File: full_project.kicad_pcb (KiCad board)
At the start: 2 copper layers, 61.4 x 86.1 mm, 40 parts, among them J1 Conn_01x16, J12 V_OFFSET, J14 Conn_01x02, J2 Raspberry_Pi_2_3, J3 Conn_01x08, J4 Screw_Terminal_01x04_titrator, J5 RF_Shield_Two_Pieces, J6 BNC_Jack, J8 Screw_Terminal_01x03, Q1 PN2222A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

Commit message: here
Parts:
- moved J6 0.77 mm to (128.0, 54.7)
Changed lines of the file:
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@@
   )
   (module Titrator_Footprints:BNC_Jack (layer F.Cu)
-    (at 127.254 54.737)
+    (at 128.025 54.675)
     (fp_text reference J6 (at 6.394 -0.443) (layer F.SilkS)
       (effects (font (size 1 1) (thickness 0.15)))
@@
   (gr_line (start 136.398 55.372) (end 136.398 27.305) (layer Dwgs.User) (width 0.15))
   (gr_line (start 161.925 27.305) (end 161.925 55.372) (layer Dwgs.User) (width 0.15))
-  (gr_line (start 161.925 55.372) (end 136.525 55.372) (layer Dwgs.User) (width 0.15))
-  (gr_line (start 188.468 55.372) (end 163.068 55.372) (layer Dwgs.User) (width 0.15))
+  (gr_line (start 161.925 55.372) (end 136.398 55.372) (layer Dwgs.User) (width 0.15))
+  (gr_line (start 188.468 55.372) (end 162.941 55.372) (layer Dwgs.User) (width 0.15))
   (gr_line (start 188.468 27.305) (end 188.468 55.372) (layer Dwgs.User) (width 0.15))
   (gr_line (start 162.941 27.305) (end 188.341 27.305) (layer Dwgs.User) (width 0.15))

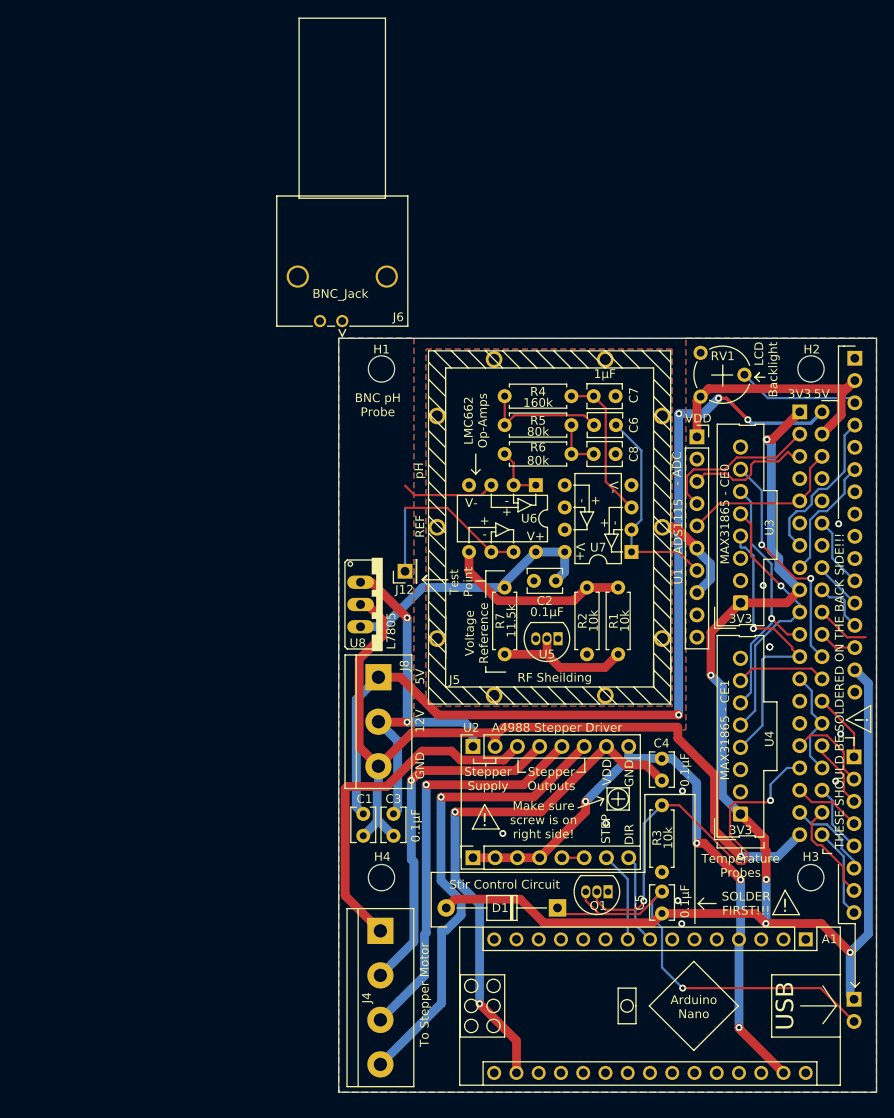
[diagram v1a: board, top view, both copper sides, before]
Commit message: Extended board, added MAX31685 footprint for new mounting style, added 3.5mm audio jacks, cried a little
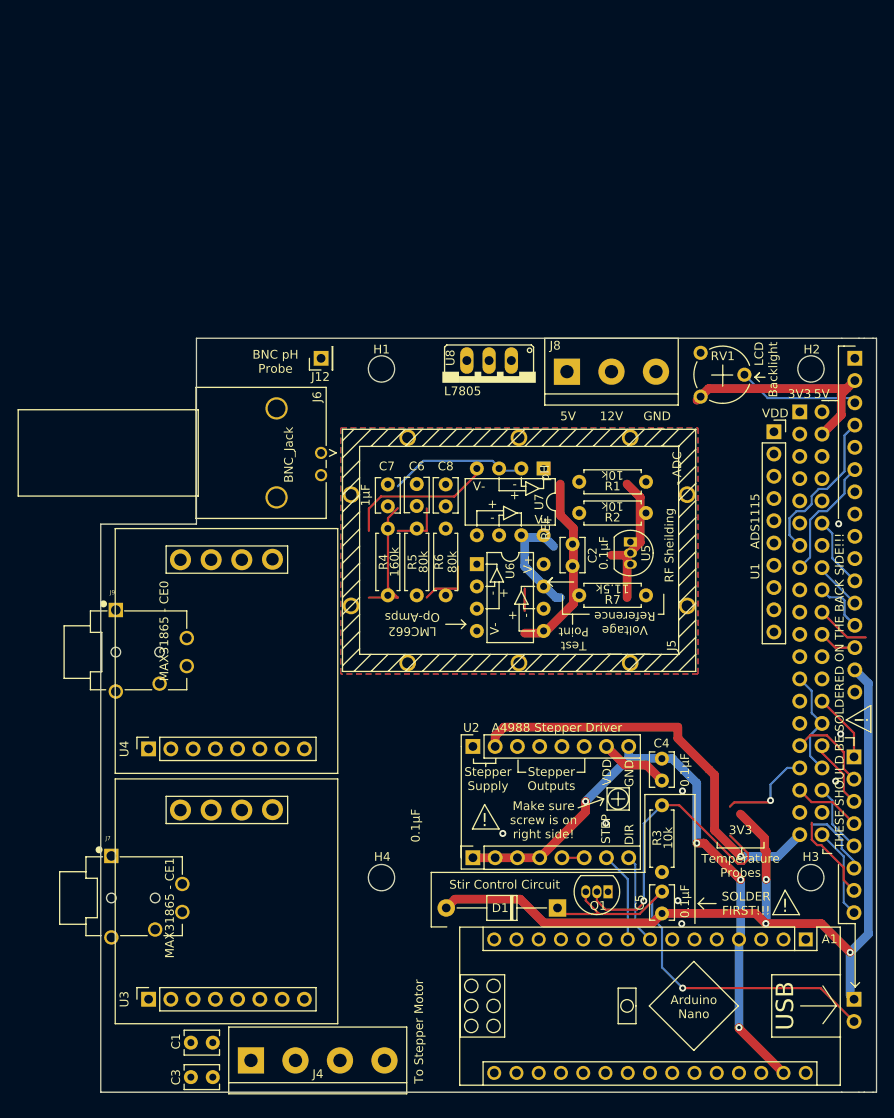
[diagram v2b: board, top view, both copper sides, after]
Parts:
- added J7: SJ-43515TS, Titrator_Footprints:CUI_SJ-43515TS, F.Cu at (104.3, 120.5)
- added J9: SJ-43515TS, Titrator_Footprints:CUI_SJ-43515TS, F.Cu at (104.8, 92.5)
- U3, U4: footprint Connector_Molex:Molex_SL_171971-0008_1x08_P2.54mm_Vertical -> Titrator_Footprints:MAX31865
- moved U3 74.1 mm to (114.8, 132.1)
- moved U4 59.1 mm to (114.8, 103.5)
- moved J8 41.0 mm to (153.7, 60.5), turned to 0 degrees
- moved C3 37.9 mm to (110.7, 141.0), turned to 0 degrees
- moved C1 32.7 mm to (110.7, 137.0), turned to 0 degrees
- moved U8 28.1 mm to (144.8, 61.7), turned to 180 degrees
- moved C7 26.6 mm to (133.2, 75.8), turned to 90 degrees
- moved J12 26.1 mm to (125.6, 58.9)
- moved R4 25.8 mm to (133.2, 78.4), turned to 270 degrees
- moved C6 23.7 mm to (136.5, 73.3), turned to 270 degrees
- moved R5 21.9 mm to (136.5, 86.0), turned to 90 degrees
- moved J4 20.9 mm to (117.6, 139.1), turned to 0 degrees
- moved R1 19.9 mm to (162.7, 73.0), turned to 180 degrees
- moved C8 17.9 mm to (139.8, 75.8), turned to 90 degrees
- moved R6 16.7 mm to (139.8, 78.4), turned to 270 degrees
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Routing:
- net /PSU_5V: track 106.3 -> 0.00 mm, vias 4 -> 0
- net +3V3: track 161.0 -> 102.9 mm, vias 5 -> 3
- net Net-(J4-Pad4): track 54.3 -> 0.00 mm, vias 1 -> 0
- net /Arduino_VDD: track 61.0 -> 7.94 mm, vias 2 -> 0
- net /PSU_GND: track 96.2 -> 48.0 mm
- net Net-(J4-Pad3): track 46.3 -> 0.00 mm, vias 1 -> 0
- net /PSU_12V: track 43.5 -> 0.00 mm, vias 2 -> 0
- net Net-(J4-Pad1): track 40.4 -> 0.00 mm
- net Net-(J4-Pad2): track 40.2 -> 0.00 mm, vias 1 -> 0
- net /SCLK: track 33.7 -> 0.00 mm, vias 1 -> 0
- net /MISO: track 31.7 -> 0.71 mm, vias 1 -> 0
- net /MOSI: track 30.5 -> 0.00 mm, vias 1 -> 0
- net /CE0: track 26.3 -> 0.00 mm, vias 2 -> 0
- net Net-(J12-Pad1): track 21.7 -> 2.54 mm
- net GND: track 37.6 -> 18.5 mm, vias 11 -> 8
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- removed copper zone on B.Cu, net GND
- removed copper zone on F.Cu, net GND
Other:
- board size 61.4 x 86.1 mm -> 88.5 x 86.1 mm

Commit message: not much
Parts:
- added H5: MountingHole, MountingHole:MountingHole_3mm, F.Cu at (117.0, 60.1)
- added H6: MountingHole, MountingHole:MountingHole_3mm, F.Cu at (104.6, 139.1)
- added J10: Screw_Terminal_01x02, TerminalBlock:TerminalBlock_bornier-2_P5.08mm, F.Cu at (143.7, 60.8)
- moved RV1 39.7 mm to (170.6, 103.0)
- moved U8 24.3 mm to (169.1, 61.9)
- moved J8 5.74 mm to (159.4, 60.8), turned to 180 degrees
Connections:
- A1 pad 1: (no net) -> Net-(A1-Pad1)
- A1 pad 10: (no net) -> Net-(A1-Pad10)
- A1 pad 11: (no net) -> Net-(A1-Pad11)
- A1 pad 12: (no net) -> Net-(A1-Pad12)
- A1 pad 13: (no net) -> Net-(A1-Pad13)
- A1 pad 14: (no net) -> Net-(A1-Pad14)
- A1 pad 15: (no net) -> Net-(A1-Pad15)
- A1 pad 16: (no net) -> Net-(A1-Pad16)
- A1 pad 18: (no net) -> Net-(A1-Pad18)
- A1 pad 19: (no net) -> Net-(A1-Pad19)
- A1 pad 2: (no net) -> Net-(A1-Pad2)
- A1 pad 20: (no net) -> Net-(A1-Pad20)
- A1 pad 21: (no net) -> Net-(A1-Pad21)
- A1 pad 22: (no net) -> Net-(A1-Pad22)
- A1 pad 23: (no net) -> Net-(A1-Pad23)
- A1 pad 24: (no net) -> Net-(A1-Pad24)
- A1 pad 25: (no net) -> Net-(A1-Pad25)
- A1 pad 26: (no net) -> Net-(A1-Pad26)
- A1 pad 27: (no net) -> Net-(A1-Pad27)
- A1 pad 28: (no net) -> Net-(A1-Pad28)
- A1 pad 3: (no net) -> Net-(A1-Pad3)
- A1 pad 30: (no net) -> Net-(A1-Pad30)
- A1 pad 5: (no net) -> Net-(A1-Pad5)
- A1 pad 6: (no net) -> Net-(A1-Pad6)
- A1 pad 7: (no net) -> Net-(A1-Pad7)
- J1 pad 10: (no net) -> Net-(J1-Pad10)
- J1 pad 7: (no net) -> Net-(J1-Pad7)
- J1 pad 8: (no net) -> Net-(J1-Pad8)
- J1 pad 9: (no net) -> Net-(J1-Pad9)
- J2 pad 10: (no net) -> Net-(J2-Pad10)
- J2 pad 11: (no net) -> Net-(J2-Pad11)
- J2 pad 27: (no net) -> Net-(J2-Pad27)
- J2 pad 29: (no net) -> /KeyRow_3
- J2 pad 32: /KeyRow_3 -> Net-(J10-Pad1)
- J2 pad 7: (no net) -> Net-(J2-Pad7)
- J2 pad 8: (no net) -> Net-(J2-Pad8)
- J6 pad 3: (no net) -> Net-(J6-Pad3)
- J6 pad 4: (no net) -> Net-(J6-Pad4)
- J7 pad 5: (no net) -> Net-(J7-Pad5)
- J9 pad 5: (no net) -> Net-(J9-Pad5)
- U1 pad 10: (no net) -> Net-(U1-Pad10)
- U1 pad 9: (no net) -> Net-(U1-Pad9)
- U3 pad 3: (no net) -> Net-(U3-Pad3)
- U3 pad 8: (no net) -> Net-(U3-Pad8)
- U4 pad 3: (no net) -> Net-(U4-Pad3)
- U4 pad 8: (no net) -> Net-(U4-Pad8)
- U5 pad 3: (no net) -> Net-(U5-Pad3)
- U7 pad 5: (no net) -> Net-(U7-Pad5)
- U7 pad 6: (no net) -> Net-(U7-Pad6)
- U7 pad 7: (no net) -> Net-(U7-Pad7)
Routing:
- net +5V: track 26.6 -> 9.56 mm

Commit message: It works now, fix any complaints
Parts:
- moved C3 97.6 mm to (163.9, 59.1)
- moved C1 91.6 mm to (163.9, 62.5)
- moved H5 24.9 mm to (103.9, 81.3)
- moved C7 18.9 mm to (146.6, 89.1), turned to 0 degrees
- moved C6 17.8 mm to (149.1, 85.8), turned to 180 degrees
- moved R4 15.2 mm to (144.0, 89.1), turned to 180 degrees
- moved C8 9.55 mm to (146.6, 82.5), turned to 0 degrees
- moved R6 5.93 mm to (144.1, 82.5), turned to 180 degrees
- moved U6 5.85 mm to (139.1, 78.5), turned to 180 degrees
- moved U8 3.97 mm to (173.0, 62.6)
- moved U1 1.84 mm to (176.2, 65.8)
- moved R5 0.21 mm to (136.4, 85.8), turned to 0 degrees
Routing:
- net +3V3: track 102.9 -> 260.7 mm, vias 3 -> 4
- net /PSU_12V: track 0.00 -> 142.0 mm, vias 0 -> 5
- net /MOSI: track 0.00 -> 105.3 mm, vias 0 -> 3
- net /SCLK: track 0.00 -> 103.7 mm, vias 0 -> 2
- net /CE0: track 0.00 -> 103.6 mm, vias 0 -> 4
- net /MISO: track 0.71 -> 102.5 mm, vias 0 -> 1
- net /PSU_GND: track 48.0 -> 138.8 mm, vias 1 -> 3
- net Net-(J10-Pad1): track 0.00 -> 84.6 mm, vias 0 -> 5
- net /CE1: track 0.00 -> 66.8 mm
- net Net-(J4-Pad1): track 0.00 -> 58.7 mm, vias 0 -> 1
- net /PSU_A5V: track 12.6 -> 70.2 mm, vias 0 -> 1
- net GND: track 18.5 -> 75.7 mm, vias 8 -> 24
- net Net-(J4-Pad2): track 0.00 -> 56.4 mm, vias 0 -> 1
- net Net-(J4-Pad3): track 0.00 -> 54.8 mm, vias 0 -> 1
- net Net-(J4-Pad4): track 0.00 -> 51.2 mm, vias 0 -> 1
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- added copper zone on B.Cu, net GND
- added copper zone on F.Cu, net GND
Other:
- board text removed: "LCD Backlight"

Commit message: filled in zone and remade interactive BOM
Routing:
- net GND: vias 24 -> 28

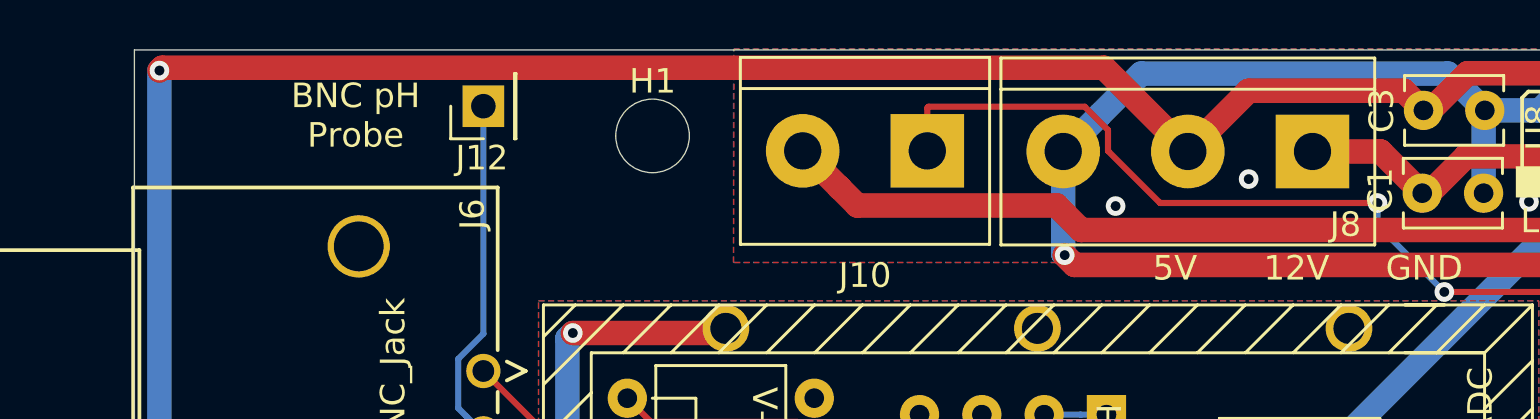
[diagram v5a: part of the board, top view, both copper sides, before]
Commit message: Added in screw terminal 3d models, adjusted screw terminal position slightly, generated gerbers
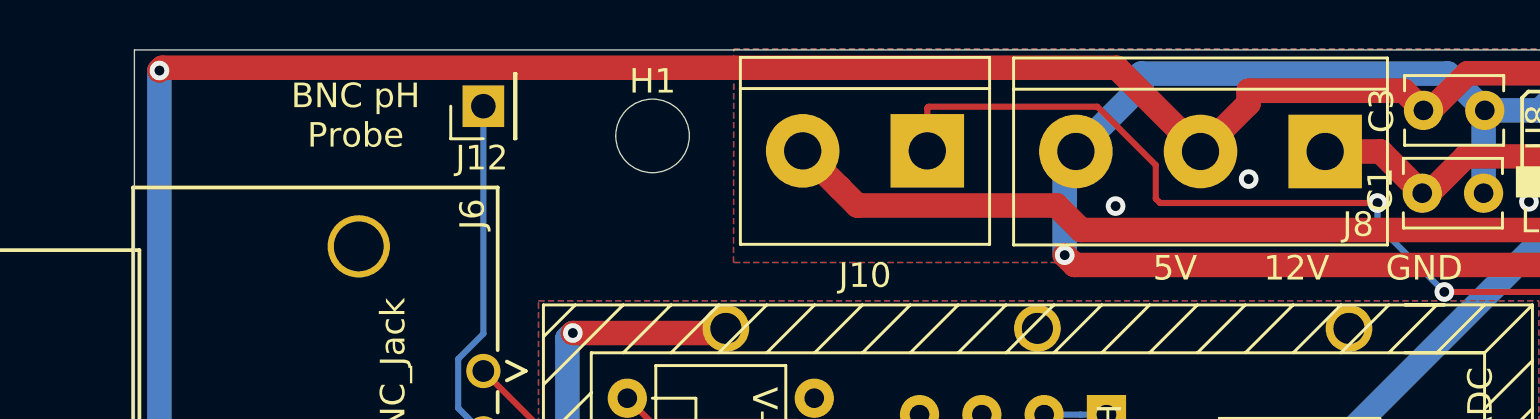
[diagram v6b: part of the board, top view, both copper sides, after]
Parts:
- moved J8 0.52 mm to (159.9, 60.8)
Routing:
- net /PSU_5V: track 27.1 -> 26.6 mm
